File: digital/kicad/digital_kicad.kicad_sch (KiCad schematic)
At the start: 17 parts, among them J1 Barrel_Jack_Switch, J2 Screw_Terminal_01x02, Q1 2N3904, Q2 2N3904, Q4 2N3904, SW1 SW_SPST

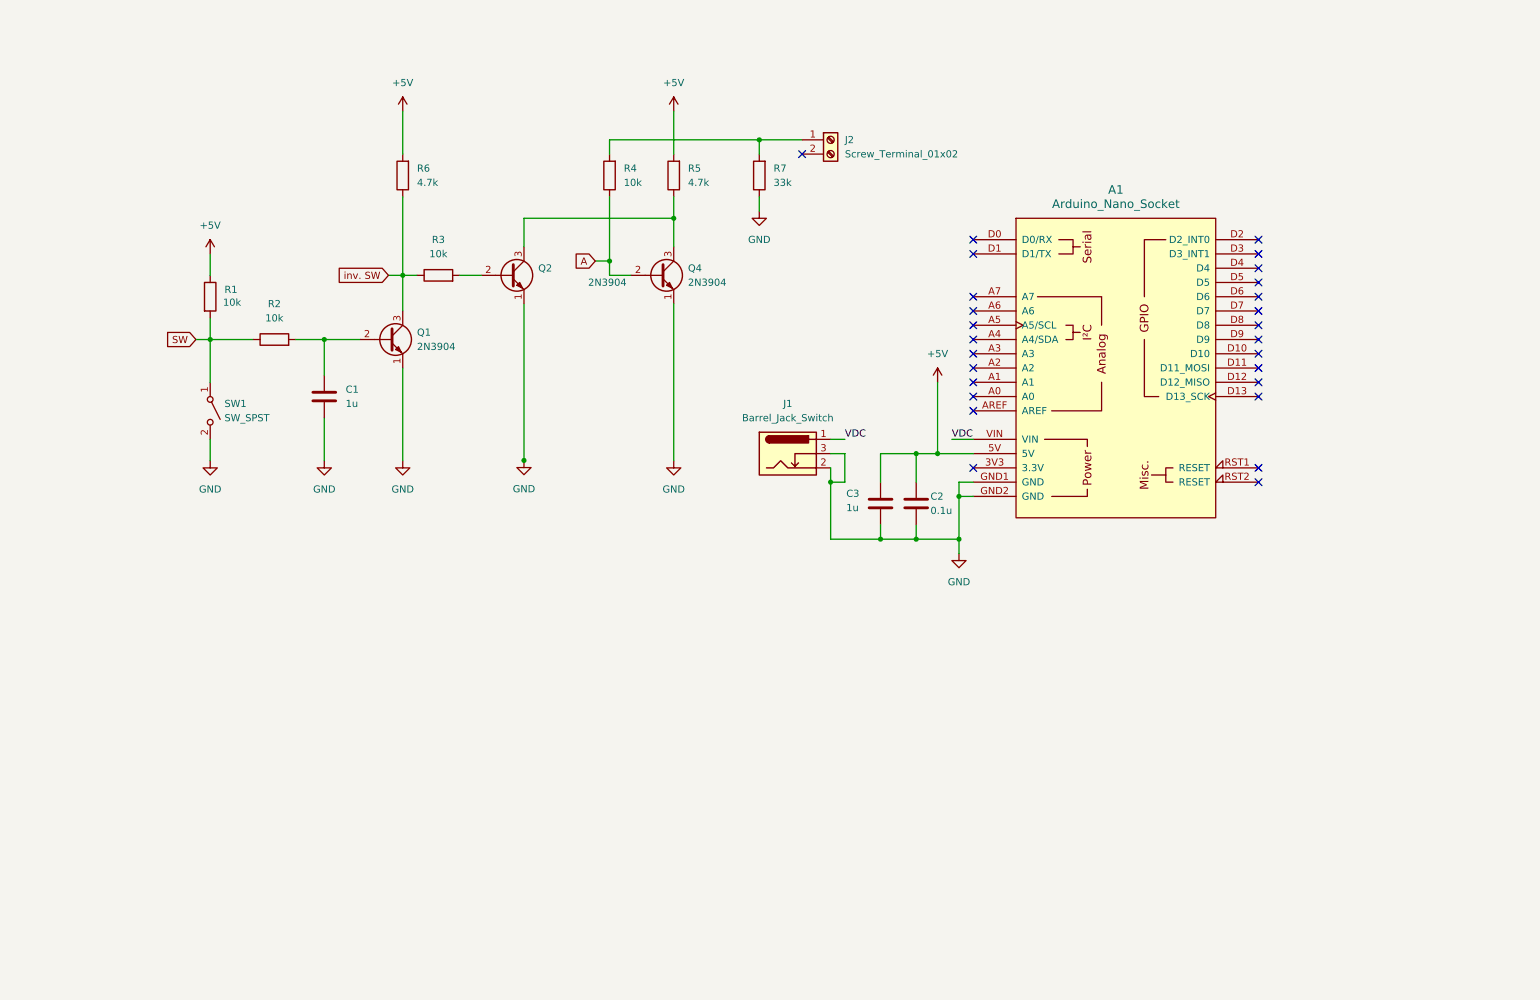
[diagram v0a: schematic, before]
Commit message: added EDS and reverse polarity protection
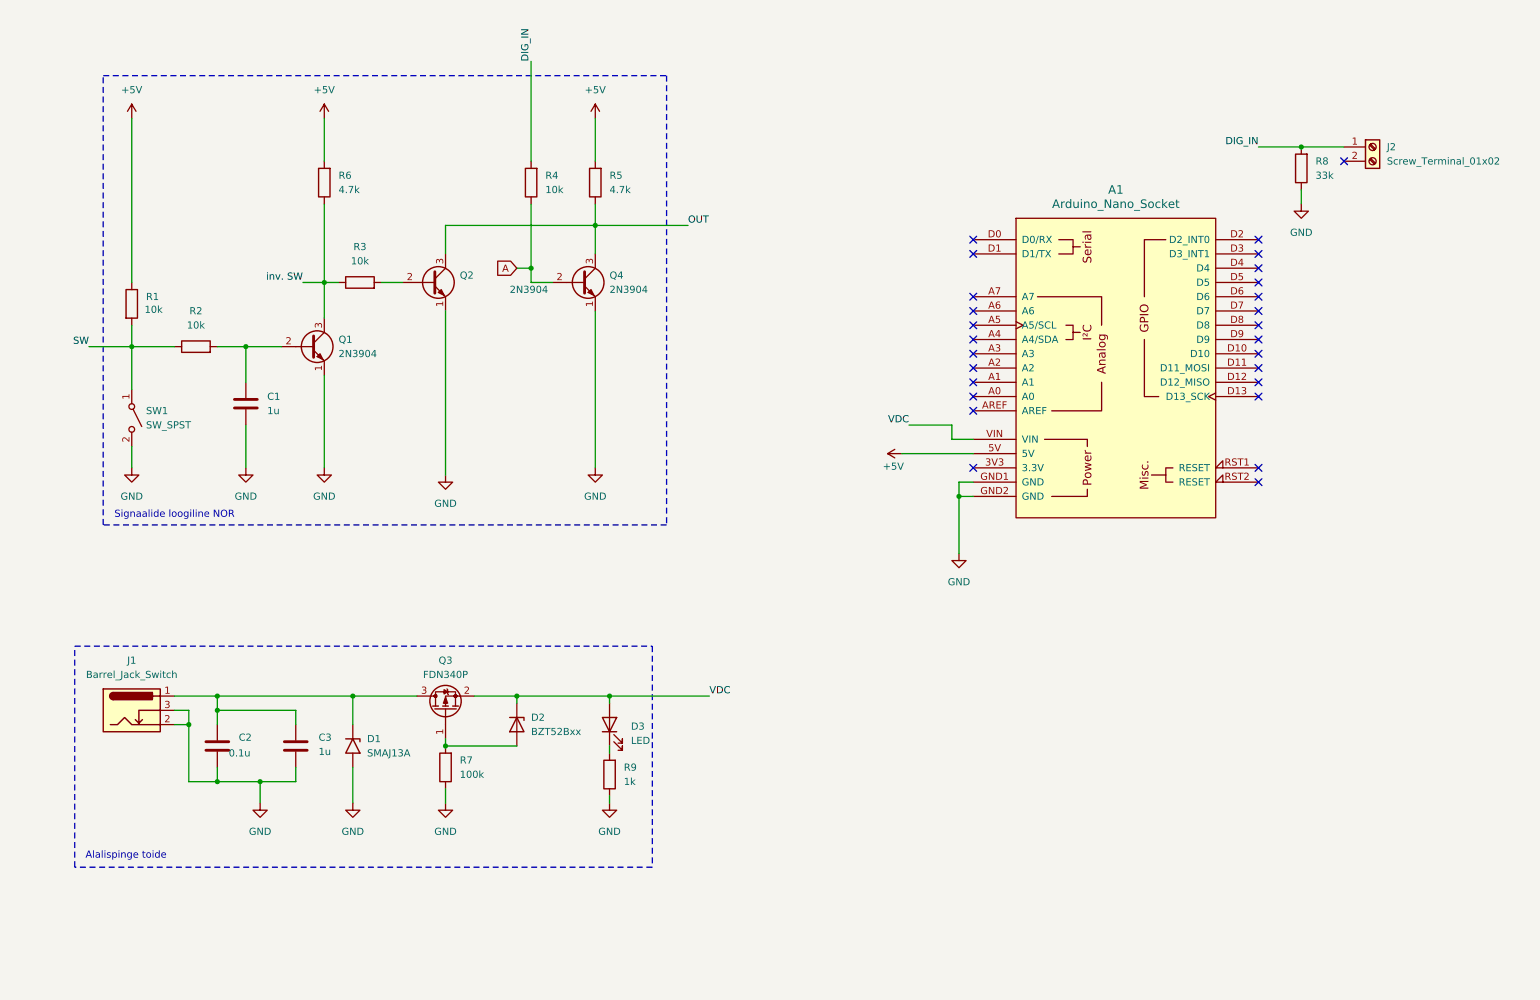
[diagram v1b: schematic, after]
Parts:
- added D1: SMAJ13A, Diode_SMD:D_SMA, symbol Diode:SMAJ13A
- added D2: BZT52Bxx, Diode_SMD:D_SOD-123F, symbol Diode:BZT52Bxx
- added D3: LED, symbol Device:LED
- added Q3: FDN340P, Package_TO_SOT_SMD:SOT-23, symbol Transistor_FET:FDN340P
- added R8: 33k, Resistor_SMD:R_0805_2012Metric_Pad1.20x1.40mm_HandSolder, symbol Device:R
- added R9: 1k, Resistor_SMD:R_0805_2012Metric_Pad1.20x1.40mm_HandSolder, symbol Device:R
- R7: value 33k -> 100k
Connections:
- net +5V: no longer C2.1, C3.1
- net GND: now also D1.2 (A2), R8.1, R9.1
- net VDC: now also D2.1 (K), D3.2 (A), Q3.2 (S); no longer J1.1
- net DIG_IN: now reaches J2.1 (Pin_1), R4.2
- net DIG_IN: now also R8.2; no longer R7.2
- net OUT: now reaches Q2.3 (C), Q4.3 (C), R5.1
- new net: D3.1 (K), R9.2
- new net: D2.2 (A), Q3.1 (G), R7.2
- new net: C2.1, C3.1, D1.1 (A1), J1.1, Q3.3 (D)
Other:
- note added: "Alalispinge toide"
- note added: "Signaalide loogiline NOR"
- moved on the sheet: C1, C2, C3, J1, J2, Q1, Q2, Q4, R1, R2, R3, R4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

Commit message: updated pcb with Jarek's changes
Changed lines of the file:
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@@
-	)
-	(junction
-		(at 49.53 138.43)
-		(diameter 0)
-		(color 0 0 0 0)
 	)
 	(junction
@@
 	)
 	(junction
+		(at 63.5 135.89)
+		(diameter 0)
+		(color 0 0 0 0)
+	)
+	(junction
 		(at 119.38 135.89)
 		(diameter 0)
@@
 	(wire
 		(pts
-			(xy 63.5 138.43) (xy 63.5 140.97)
+			(xy 63.5 135.89) (xy 63.5 140.97)
 		)
 		(stroke
@@
 	(wire
 		(pts
-			(xy 49.53 135.89) (xy 73.66 135.89)
+			(xy 49.53 135.89) (xy 63.5 135.89)
 		)
 		(stroke
@@
 	(wire
 		(pts
-			(xy 49.53 138.43) (xy 49.53 140.97)
+			(xy 49.53 135.89) (xy 49.53 140.97)
 		)
 		(stroke
@@
 	(wire
 		(pts
+			(xy 63.5 135.89) (xy 73.66 135.89)
+		)
+		(stroke
+			(width 0)
+			(type default)
+		)
+	)
+	(wire
+		(pts
 			(xy 102.87 137.16) (xy 102.87 135.89)
 		)
@@
 	(wire
 		(pts
-			(xy 49.53 135.89) (xy 49.53 138.43)
-		)
-		(stroke
-			(width 0)
-			(type default)
-		)
-	)
-	(wire
-		(pts
 			(xy 63.5 151.13) (xy 57.15 151.13)
 		)
@@
 		)
 		(stroke
-			(width 0)
-			(type default)
-		)
-	)
-	(wire
-		(pts
-			(xy 49.53 138.43) (xy 63.5 138.43)
-		)
-		(stroke

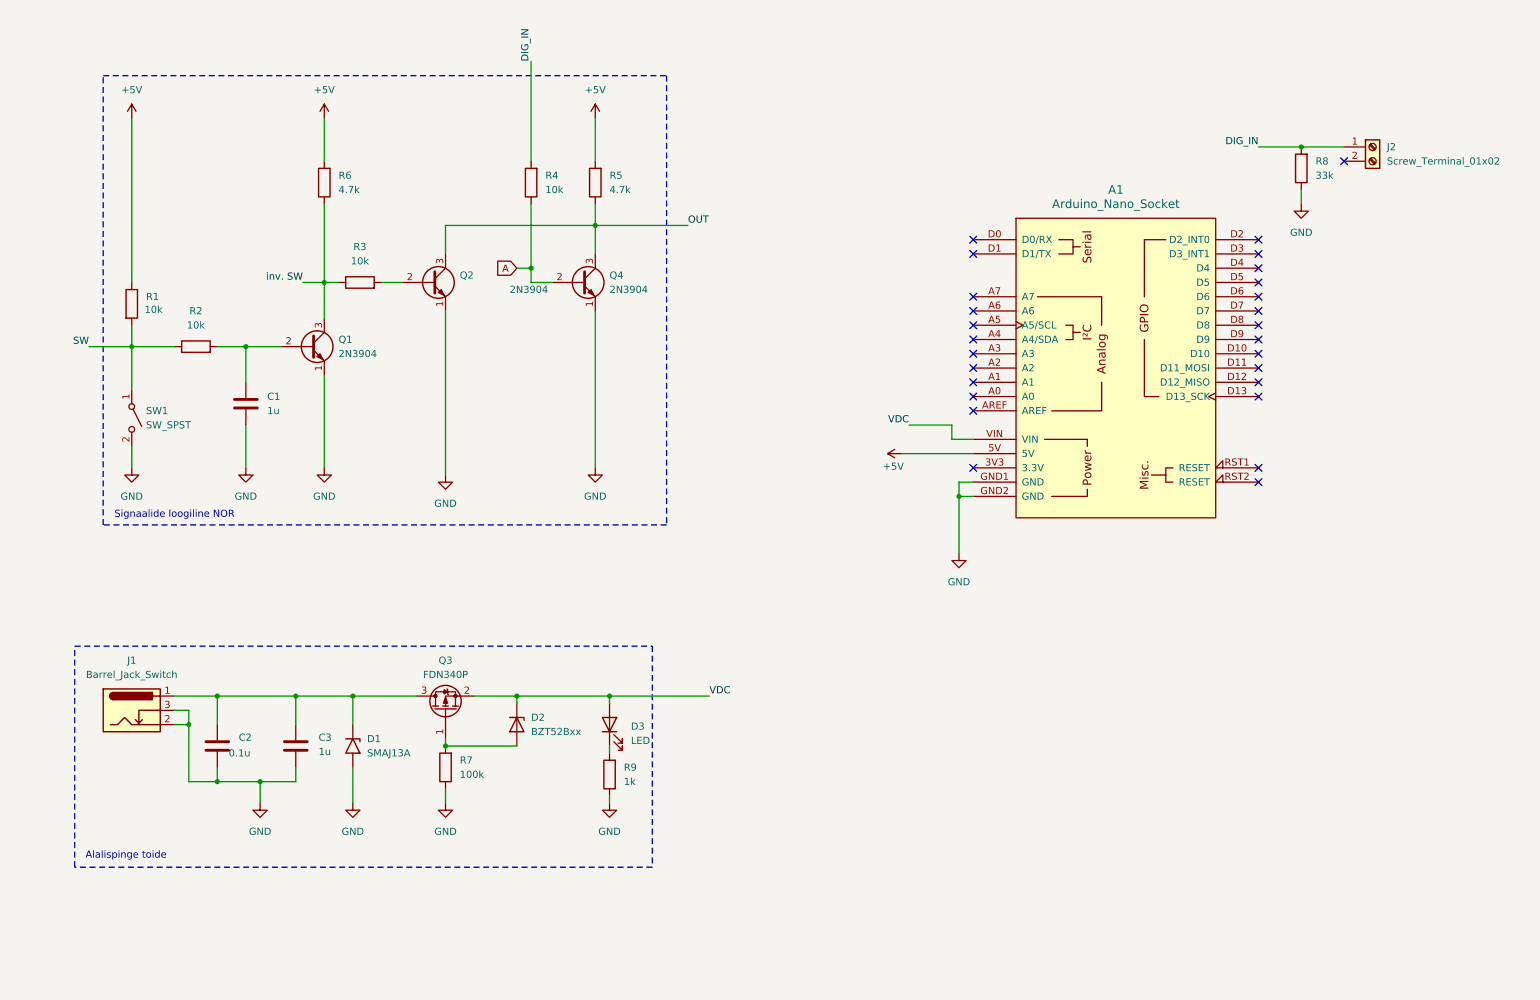
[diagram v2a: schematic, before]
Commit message: redid the digital schematic to be more compact
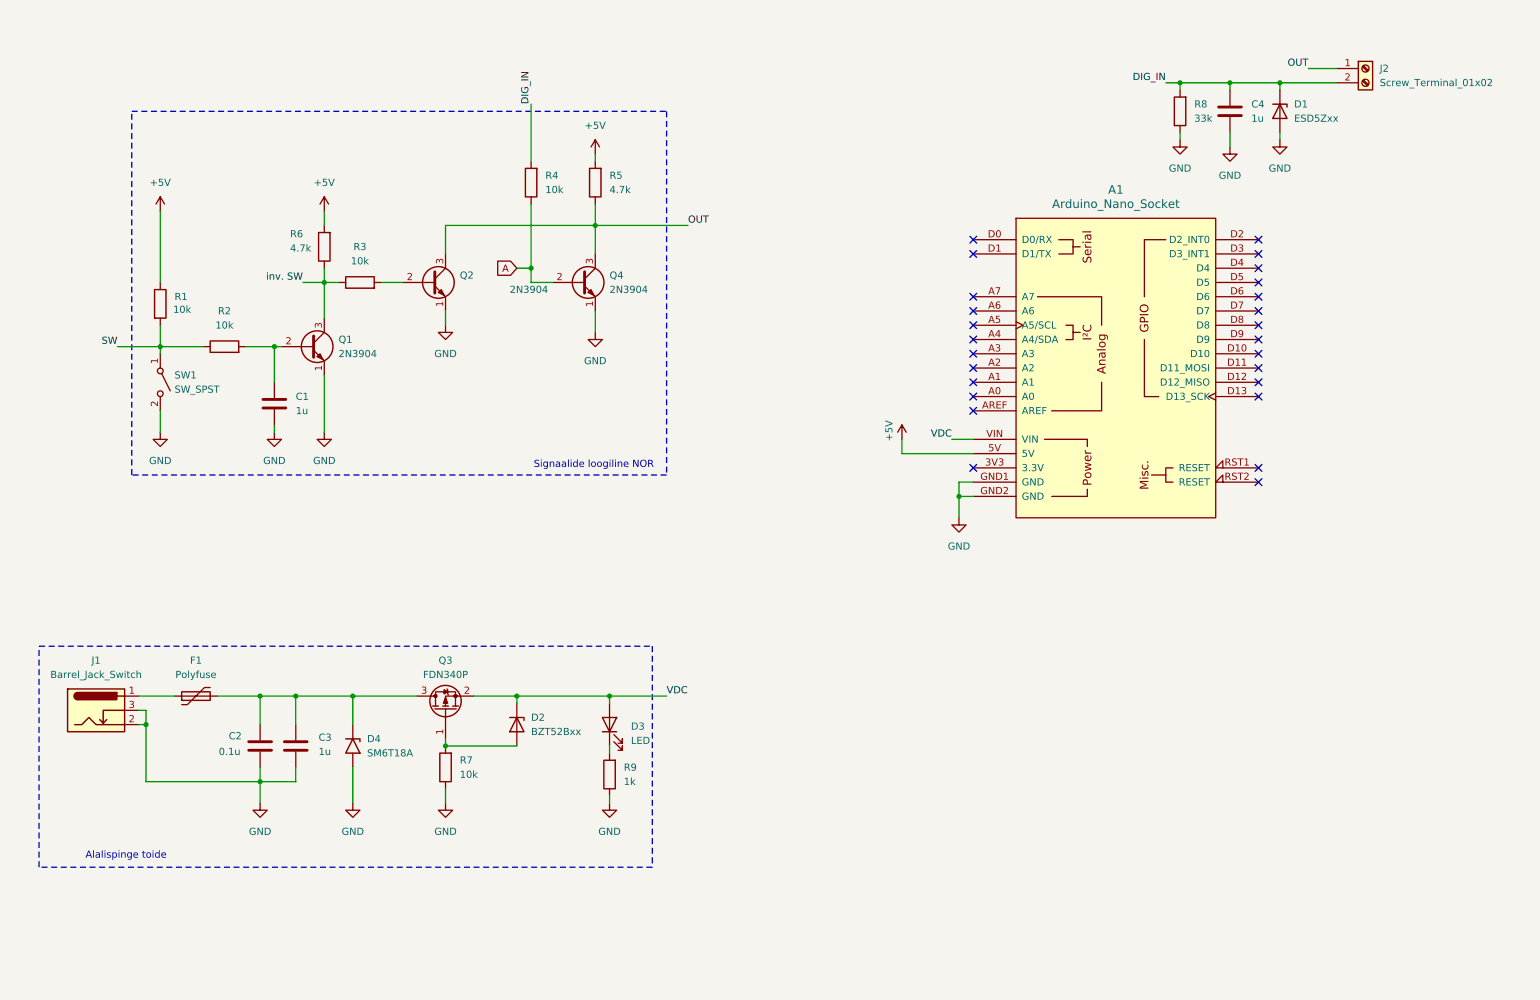
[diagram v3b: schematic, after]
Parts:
- removed D1: SMAJ13A, Diode_SMD:D_SMA, symbol Diode:SMAJ13A
- added C4: 1u, Capacitor_SMD:C_0805_2012Metric_Pad1.18x1.45mm_HandSolder, symbol Device:C
- added D1: ESD5Zxx, Diode_SMD:D_SOD-523, symbol Diode:ESD5Zxx
- added D4: SM6T18A, Diode_SMD:D_SMB, symbol Diode:SM6T18A
- added F1: Polyfuse, Fuse:Fuse_1206_3216Metric_Pad1.42x1.75mm_HandSolder, symbol Device:Polyfuse
- D3: footprint (none) -> LED_SMD:LED_0805_2012Metric_Pad1.15x1.40mm_HandSolder
- J1: footprint Connector_BarrelJack:BarrelJack_Wuerth_6941xx301002 -> Connector_BarrelJack:BarrelJack_Horizontal
- R7: value 100k -> 10k
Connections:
- net DIG_IN: now also J2.2 (Pin_2), C4.1, D1.1 (K); no longer J2.1 (Pin_1)
- net GND: now also C4.2, D1.2 (A), D4.2 (A2)
- net OUT: now also J2.1 (Pin_1)
- net at C2.1, C3.1, Q3.3 (D): now also D4.1 (A1), F1.2; no longer J1.1
- new net: F1.1, J1.1
- no-connect marks 27 -> 26
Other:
- moved on the sheet: C1, C2, J1, J2, R1, R2, R6, R8, SW1

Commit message: fixed pcb silkscreen, added power switch
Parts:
- added SW2: SW_Nidec_CAS-120A1, Button_Switch_SMD:Nidec_Copal_CAS-120A, symbol Switch:SW_Nidec_CAS-120A1
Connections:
- net GND: now also SW2.3 (A)
- net at J1.1: now also SW2.1 (C); no longer F1.1
- new net: F1.1, SW2.2 (B)
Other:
- moved on the sheet: C2, C3, D2, D3, D4, F1, Q3, R7, R9
